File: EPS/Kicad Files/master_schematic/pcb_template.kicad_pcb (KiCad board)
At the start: 2 copper layers, 96 x 90 mm, 5 parts, among them J1 THD-20-R

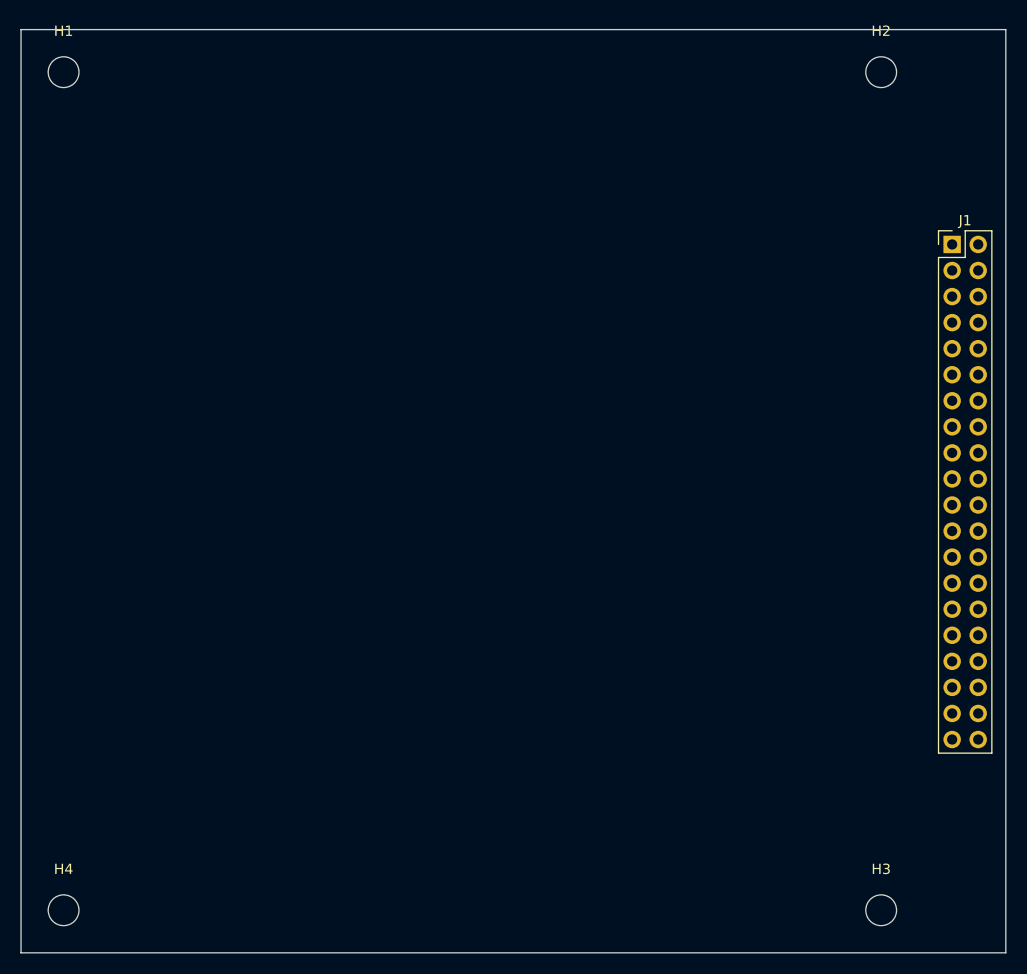
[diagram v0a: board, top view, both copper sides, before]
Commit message: revised EPS schematics
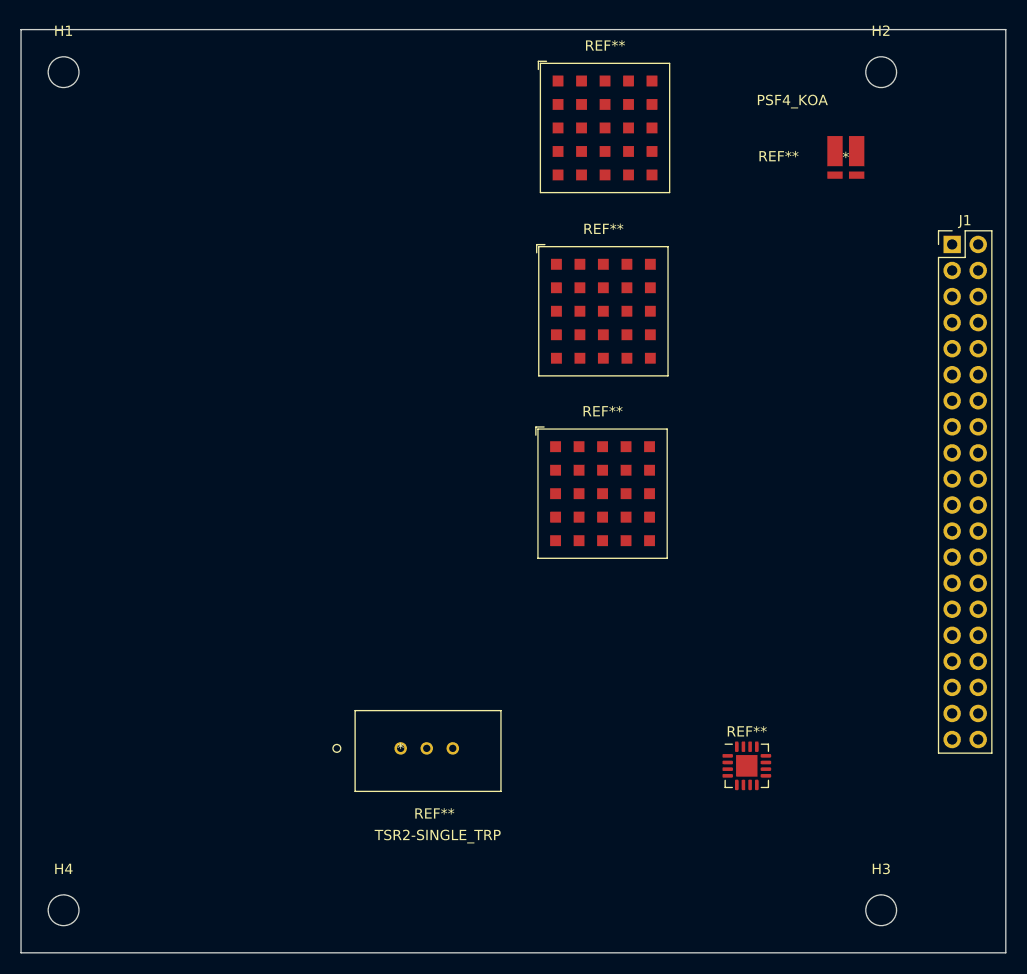
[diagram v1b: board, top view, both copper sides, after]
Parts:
- added REF**: PSF4_KOA, footprints2:PSF4NTEBL500F, F.Cu at (100.4, 32.5)
- added REF**: Converter_DCDC_RECOM_RPMx.x-x.0, Converter_DCDC:Converter_DCDC_RECOM_RPMx.x-x.0, F.Cu at (76.7, 65.2)
- added REF**: Texas_RGV_S-PVQFN-N16_EP2.1x2.1mm, Package_DFN_QFN:Texas_RGV_S-PVQFN-N16_EP2.1x2.1mm, F.Cu at (90.8, 91.8)
- added REF**: Converter_DCDC_RECOM_RPMx.x-x.0, Converter_DCDC:Converter_DCDC_RECOM_RPMx.x-x.0, F.Cu at (76.8, 47.5)
- added REF**: Converter_DCDC_RECOM_RPMx.x-x.0, Converter_DCDC:Converter_DCDC_RECOM_RPMx.x-x.0, F.Cu at (76.9, 29.6)
- added REF**: TSR2-SINGLE_TRP, footprints1:TSR 2-0518, F.Cu at (57.0, 90.1)
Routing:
- net +5V: track 0.00 -> 1.13 mm

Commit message: updated master schematic
should be nearing final schematic revision. run electrical rules check next
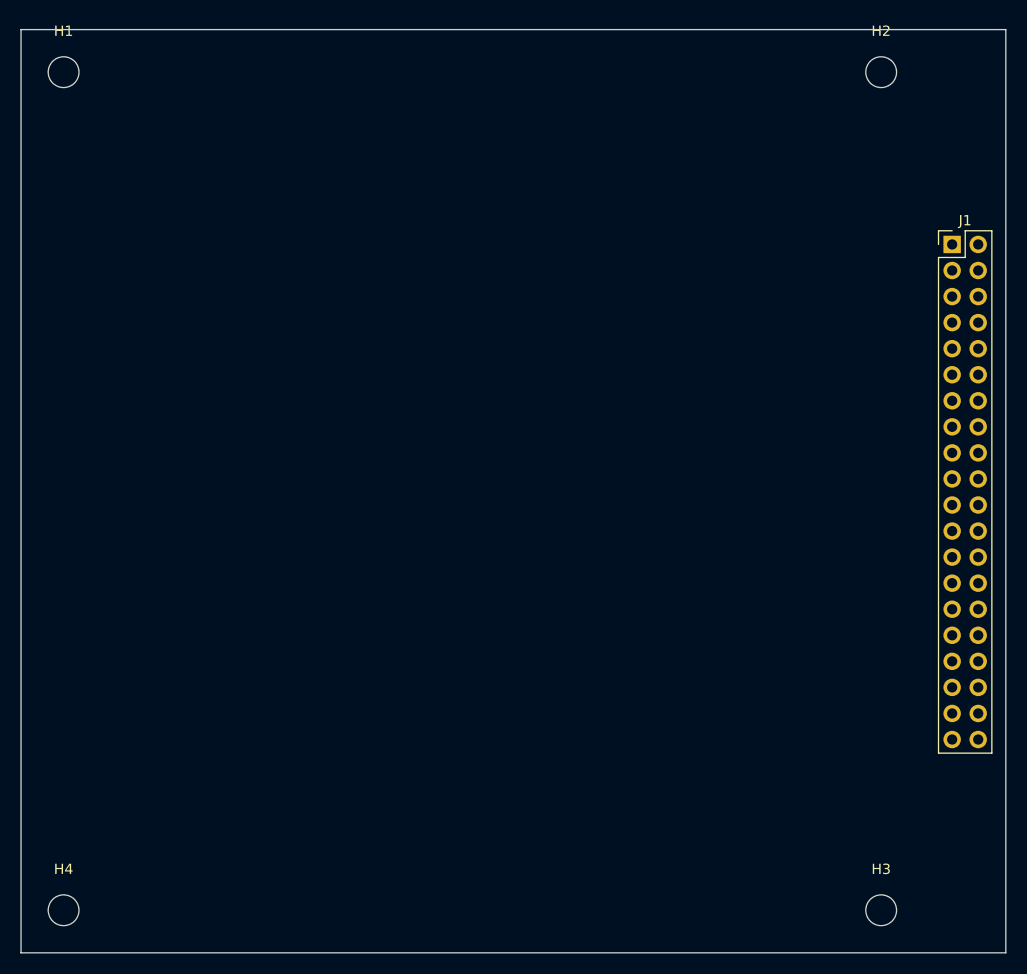
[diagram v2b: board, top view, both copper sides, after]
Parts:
- removed REF**: PSF4_KOA, footprints2:PSF4NTEBL500F
- removed REF** (x3): Converter_DCDC_RECOM_RPMx.x-x.0, Converter_DCDC:Converter_DCDC_RECOM_RPMx.x-x.0
- removed REF**: Texas_RGV_S-PVQFN-N16_EP2.1x2.1mm, Package_DFN_QFN:Texas_RGV_S-PVQFN-N16_EP2.1x2.1mm
- removed REF**: TSR2-SINGLE_TRP, footprints1:TSR 2-0518
